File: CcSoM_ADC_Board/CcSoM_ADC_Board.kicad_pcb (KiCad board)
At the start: 4 copper layers, 160 x 100 mm, 159 parts, among them J1 SoM Connector, J12 USB_C_Receptacle_USB2.0_16P, J13 Conn_02x03_Odd_Even, J14 Conn_02x03_Odd_Even, J15 Conn_02x02_Counter_Clockwise, J16 Barrel_Jack, J18 USB_A, J19 USB_A, J3 Conn_02x8_Odd_Even, J4 Conn_Coaxial, J5 HR911130A1, J6 Conn_01x14, J7 Conn_01x08, J8 Conn_01x16_Socket, J9 Conn_01x08, SW3 SW_Push, U1 SN74LVC00APWE4, U10 USB3343, U11 RTL8211E-VB-CG, U12 LTC2242IUP-12-PBF, U14 SN74CB3T3306DCTR, U2 74AUP1G04, U3 93LC46B, U4 FT2232HL, U5 SN74CB3T3245PWR, U6 TPS73625DBV, U7 TPS3307-33DR, U8 TPS73633DBV, U9 TXS0202YZPR, X1 12MHz, Y1 25MHz

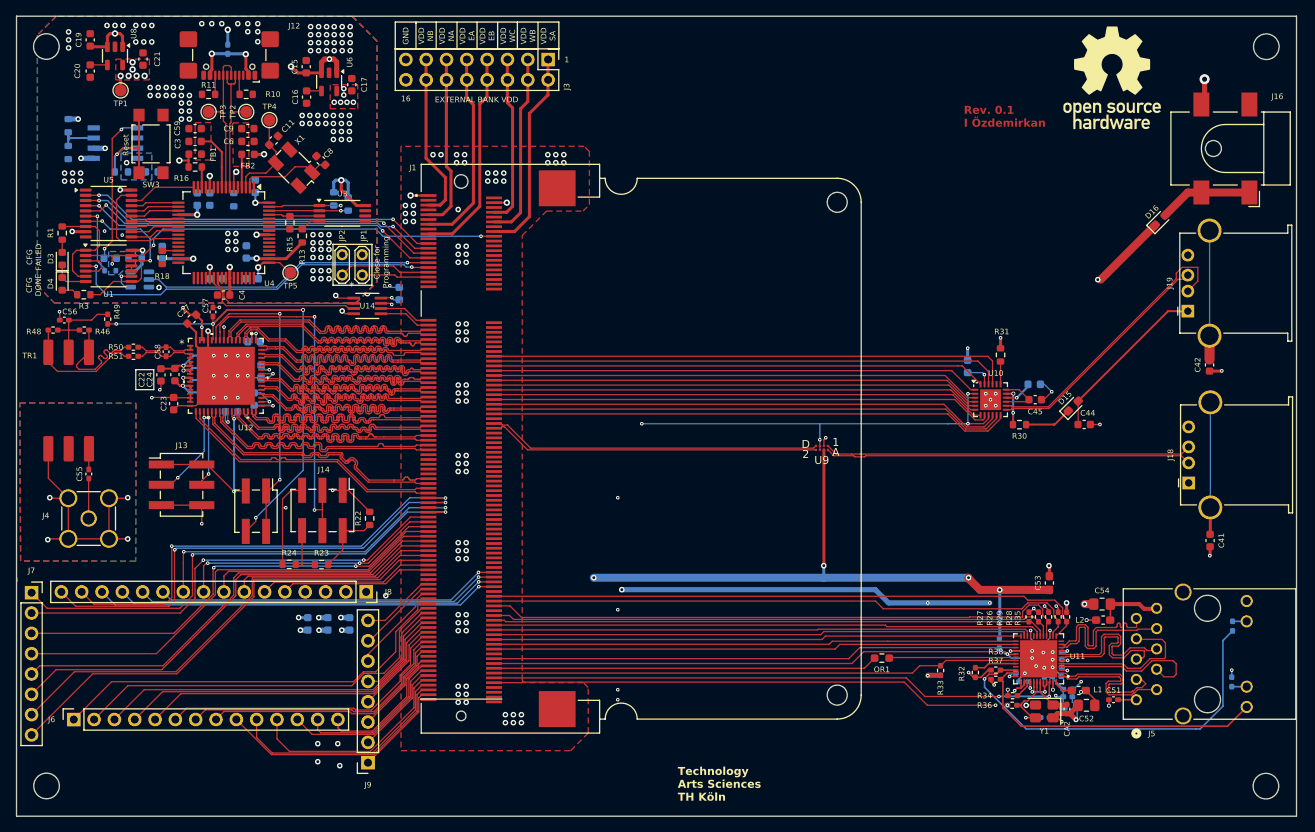
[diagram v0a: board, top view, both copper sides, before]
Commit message: changed schottky, began to add digikey part numbers
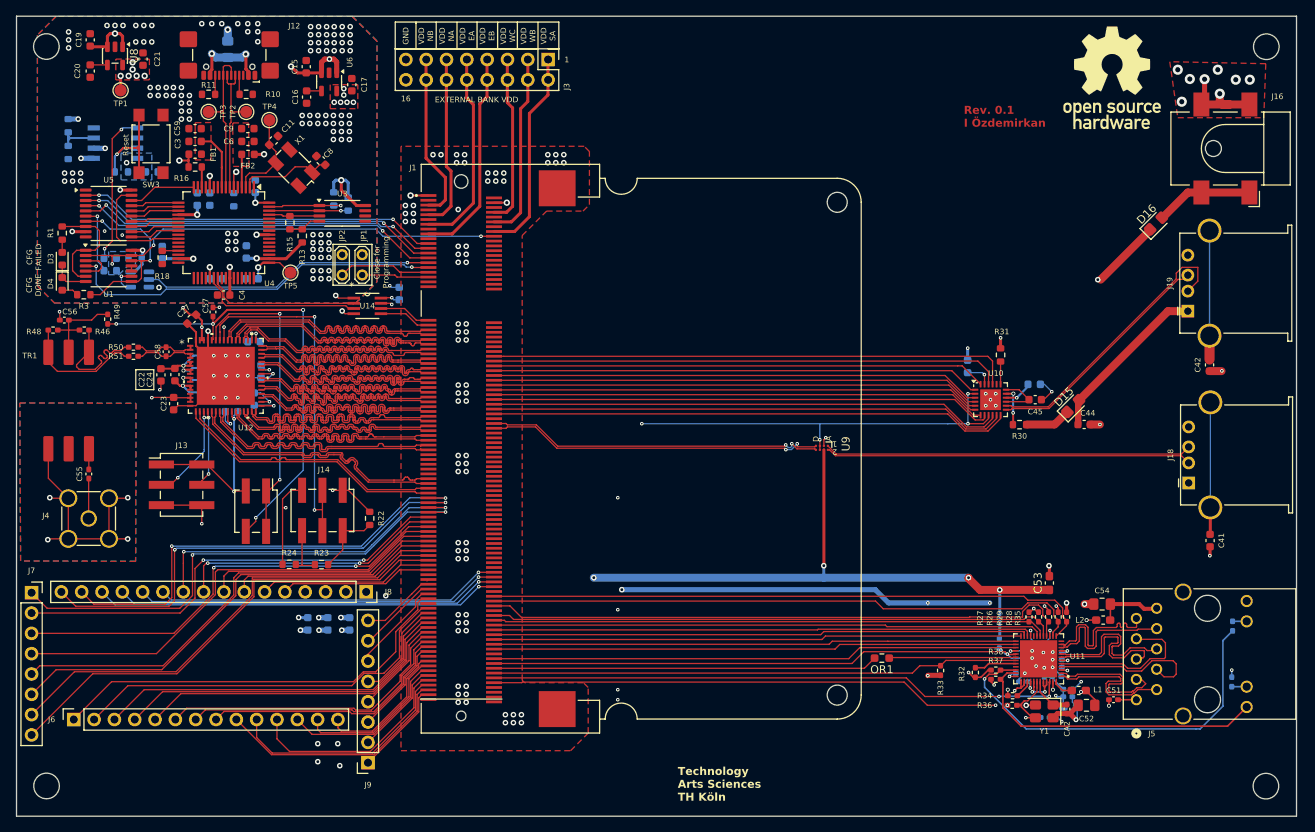
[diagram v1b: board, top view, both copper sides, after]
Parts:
- D1: footprint Diode_SMD:D_SOD-523 -> LED_SMD:LED_0603_1608Metric
- D15, D16: footprint Diode_SMD:D_0603_1608Metric_Pad1.05x0.95mm_HandSolder -> Diode_SMD:D_0805_2012Metric_Pad1.15x1.40mm_HandSolder
- D17: footprint Diode_SMD:D_0402_1005Metric_Pad0.77x0.64mm_HandSolder -> Diode_SMD:D_0805_2012Metric_Pad1.15x1.40mm_HandSolder
- moved D16 0.67 mm to (209.5, 76.5)
- turned R22 to -90 degrees
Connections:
- J16 pad 3: (no net) -> OGND
- J18 pad 2: /usb2/D_+ -> /usb2/D_-
- J18 pad 3: /usb2/D_- -> /usb2/D_+
- U9 pad A1: /usb2/D_- -> /usb2/D_+
- U9 pad A2: /usb2/D_+ -> /usb2/D_-
- U9 pad D1: USB2_- -> USB2_+
- U9 pad D2: USB2_+ -> USB2_-
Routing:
- net OGND: track 118.4 -> 128.0 mm, vias 260 -> 267
- net +5V: track 364.2 -> 362.9 mm
- net USB2_-: track 41.6 -> 42.3 mm, vias 0 -> 2
- net USB2_+: track 41.5 -> 42.2 mm, vias 0 -> 2
- net Net-(D16-A): track 12.1 -> 12.7 mm

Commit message: digikey no not complete
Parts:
- C44: value 3uF -> 3.3uF
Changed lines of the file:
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@@
 			)
 		)
-		(property "Datasheet" ""
+		(property "Datasheet" "~"
 			(at 0 0 180)
 			(layer "F.Fab")
@@
 			)
 		)
-		(property "Description" ""
+		(property "Description" "Resistor"
 			(at 0 0 180)
 			(layer "F.Fab")
@@
 			)
 		)
-		(property "Datasheet" ""
+		(property "Datasheet" "~"
 			(at 0 0 90)
 			(layer "F.Fab")
@@
 			)
 		)
-		(property "Description" ""
+		(property "Description" "Unpolarized capacitor, small symbol"
 			(at 0 0 90)
 			(layer "F.Fab")
@@
 			)
 		)
-		(property "Value" "3uF"
+		(property "Value" "3.3uF"
 			(at 0 1.43 0)
 			(layer "F.Fab")
@@
 		(tags "capacitor")
 		(property "Reference" "C43"
-			(at -0.232769 1.931116 90)
+			(at 0.017231 1.681116 90)
 			(layer "B.SilkS")
 			(effects
@@
 	)
 	(gr_text "Stackup: JLC041011-3313\n50Ohm Single-ended: 0.1427\n100Ohm differential:\n	width:0.1016 spacing:0.1524\n"
-		(at 133.2 121.45 0)
+		(at 133.2 119.25 0)
 		(layer "Cmts.User")
 		(effects

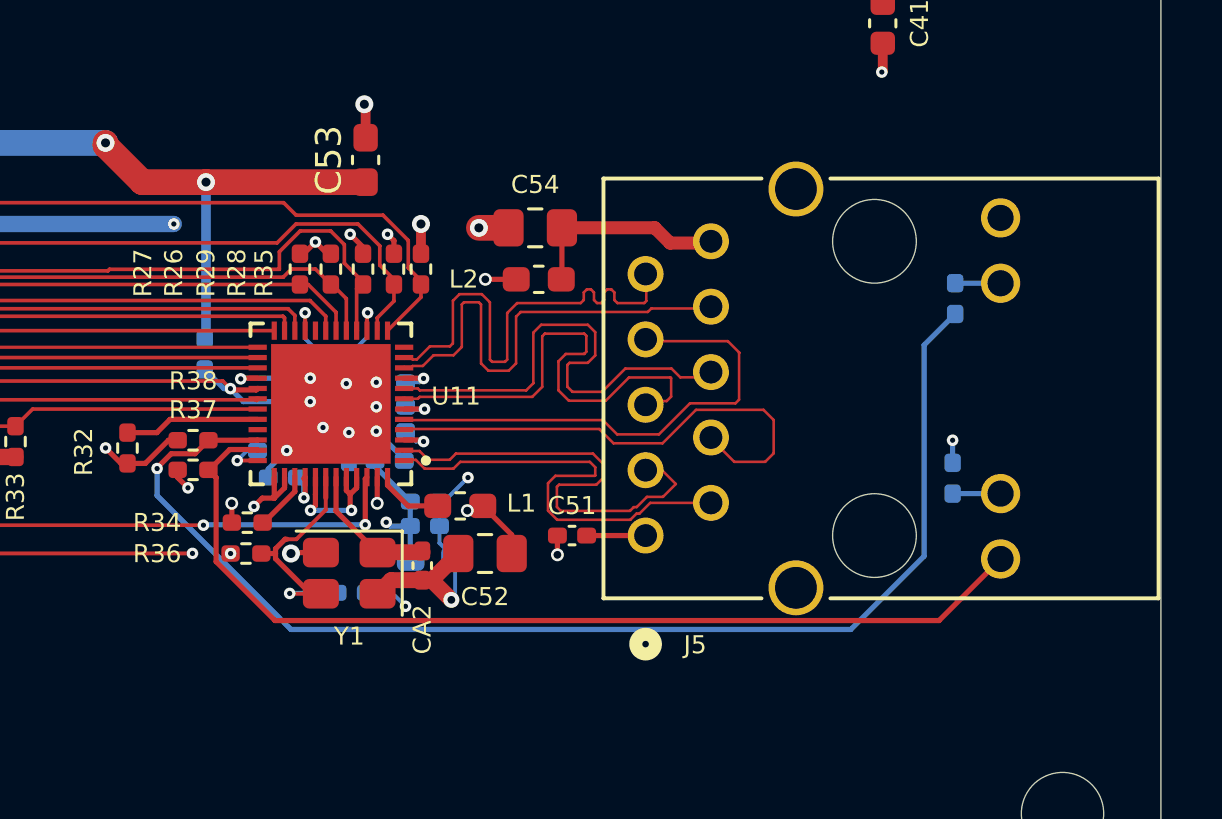
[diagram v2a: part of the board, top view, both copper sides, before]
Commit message: changed library path added symbols and footprints
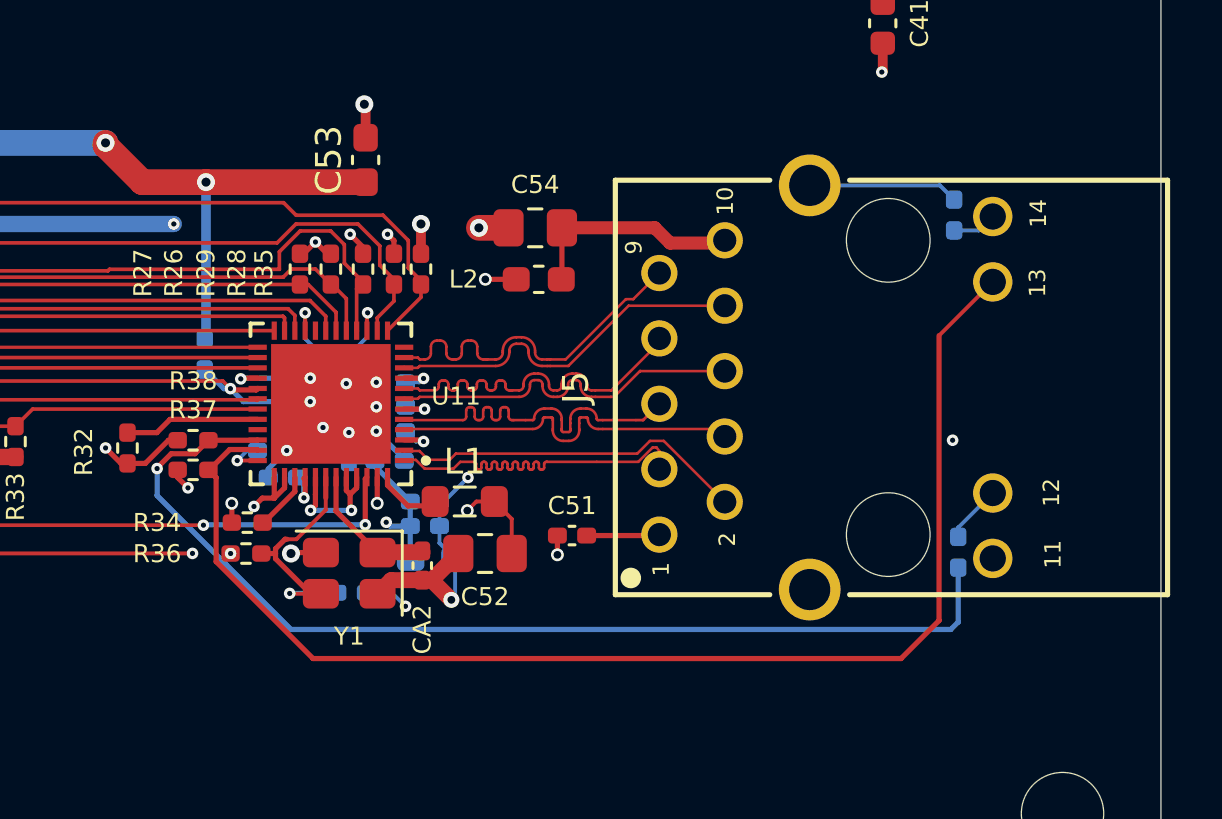
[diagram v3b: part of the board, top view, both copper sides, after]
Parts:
- removed R40: 510R R0402 5%, Resistor_SMD:R_0402_1005Metric_Pad0.72x0.64mm_HandSolder
- added R4: 510R R0402 5%, Resistor_SMD:R_0402_1005Metric_Pad0.72x0.64mm_HandSolder, B.Cu at (219.2, 136.7)
- J5: value HR911130A1 -> WE-RJ45_7498111124; footprint HR911130A1:HR911130A_HAN -> WE-RJ45_7498111124:7498111124
- L1: footprint Inductor_SMD:L_0603_1608Metric_Pad1.05x0.95mm_HandSolder -> Inductor_SMD:L_0805_2012Metric_Pad1.05x1.20mm_HandSolder
- moved J5 11.0 mm to (216.5, 130.2)
- moved R39 10.2 mm to (219.1, 123.6)
- moved L1 0.24 mm to (200.1, 134.7)
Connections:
- J5 pad 11: /gigabit_ethernet/LED1_AD1 -> +3V3
- J5 pad 12: /gigabit_ethernet/RGMII_GR- -> /gigabit_ethernet/RGMI_YE-
- J5 pad 13: /gigabit_ethernet/RGMI_YE- -> /gigabit_ethernet/LED1_AD1
- J5 pad 14: +3V3 -> /gigabit_ethernet/RGMII_GR-
- J5 pad 2: /gigabit_ethernet/MDI0_P -> /gigabit_ethernet/MDI0_N
- J5 pad 3: /gigabit_ethernet/MDI0_N -> /gigabit_ethernet/MDI0_P
- J5 pad 5: /gigabit_ethernet/MDI2_P -> /gigabit_ethernet/MDI1_N
- J5 pad 6: /gigabit_ethernet/MDI2_N -> /gigabit_ethernet/MDI2_P
- J5 pad 7: /gigabit_ethernet/MDI1_N -> /gigabit_ethernet/MDI2_N
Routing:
- net +3V3: track 469.0 -> 486.6 mm
- net /gigabit_ethernet/LED1_AD1: track 38.2 -> 50.1 mm
- net /gigabit_ethernet/LED0_AD0: track 48.5 -> 40.6 mm
- net /gigabit_ethernet/MDI1_N: track 19.5 -> 14.4 mm
- net /gigabit_ethernet/MDI1_P: track 19.5 -> 14.5 mm
- net OGND: track 128.0 -> 132.9 mm
- net /gigabit_ethernet/MDI2_N: track 19.1 -> 14.4 mm
- net /gigabit_ethernet/MDI2_P: track 19.1 -> 14.4 mm
- net /gigabit_ethernet/MDI3_N: track 18.5 -> 14.4 mm
- net /gigabit_ethernet/MDI3_P: track 18.5 -> 14.5 mm
- net /gigabit_ethernet/MDI0_N: track 18.2 -> 14.5 mm
- net /gigabit_ethernet/MDI0_P: track 17.9 -> 14.4 mm
- net VDD10_EPHY: track 30.6 -> 31.6 mm
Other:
- board text added: "U11"

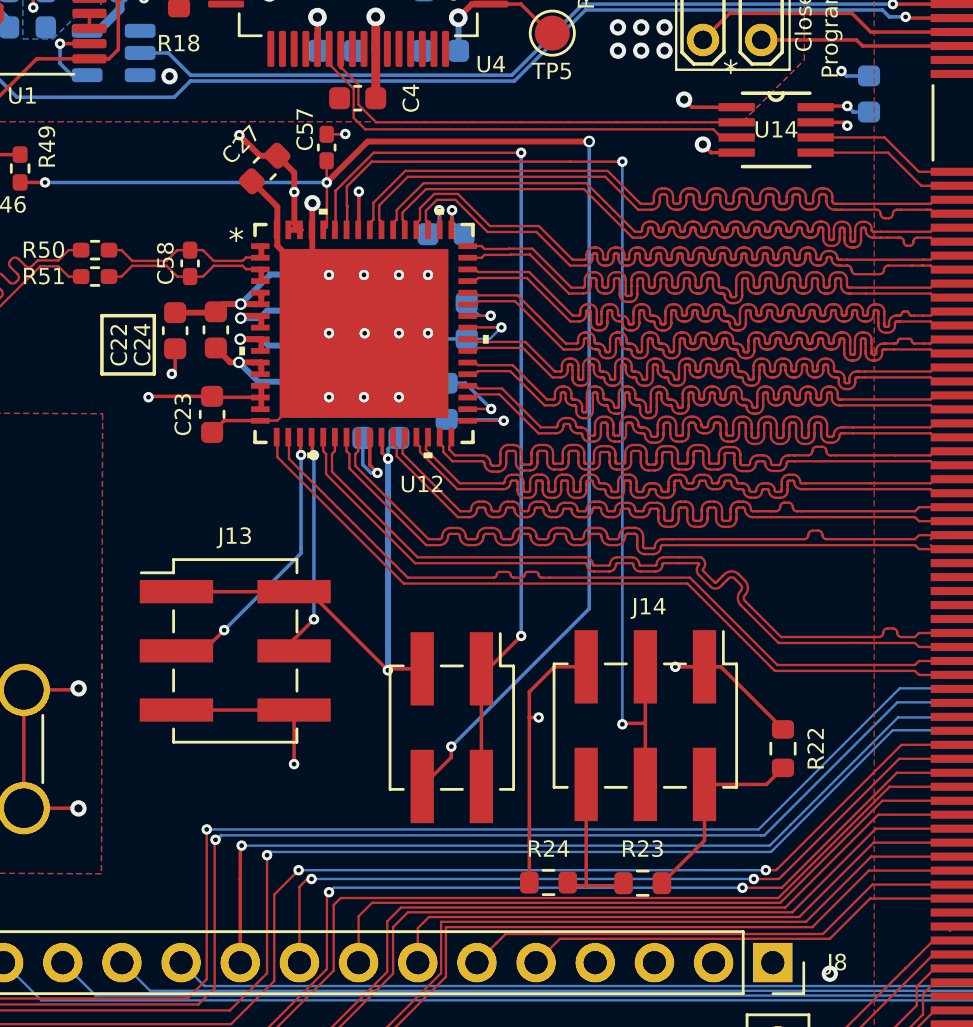
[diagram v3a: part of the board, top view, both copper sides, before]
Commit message: changed footprint of pinheader from smd to through hole
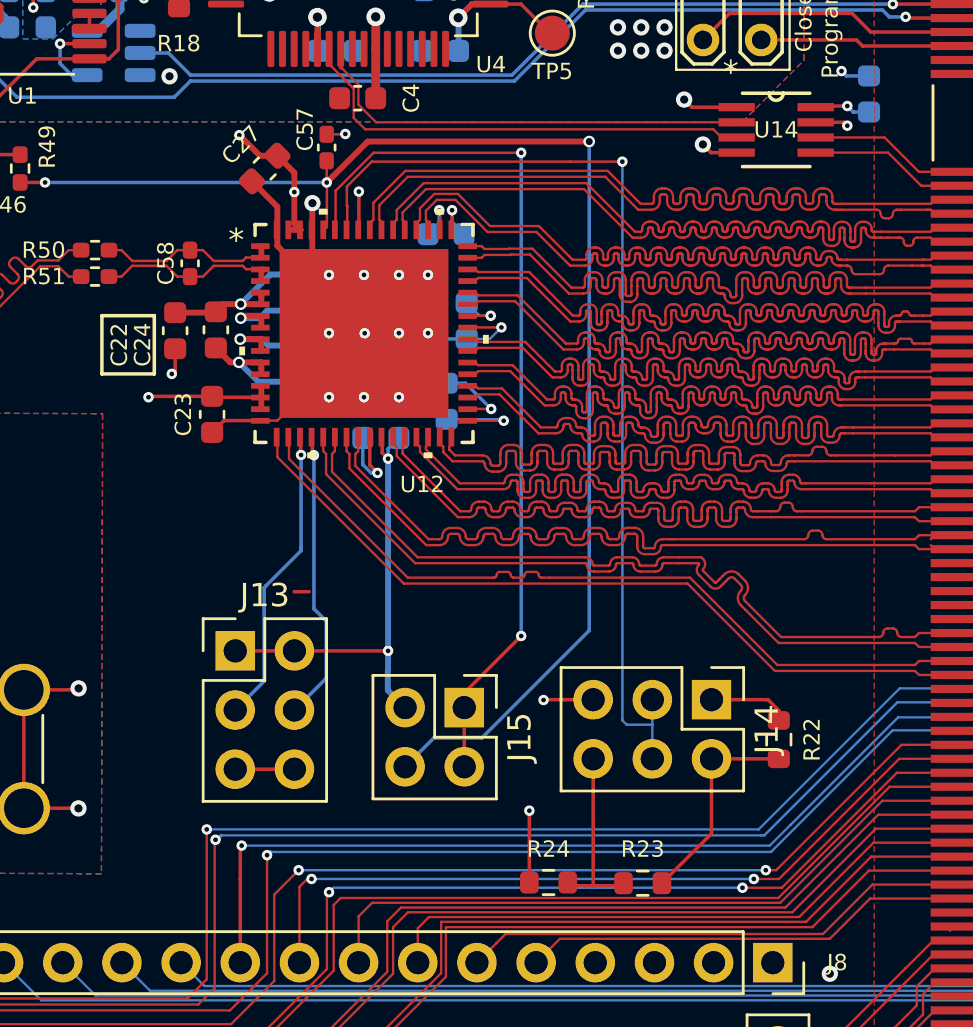
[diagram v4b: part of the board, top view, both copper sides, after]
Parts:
- J13, J14: footprint Connector_PinHeader_2.54mm:PinHeader_2x03_P2.54mm_Vertical_SMD -> Connector_PinHeader_2.54mm:PinHeader_2x03_P2.54mm_Vertical
- J15: footprint Connector_PinHeader_2.54mm:PinHeader_2x02_P2.54mm_Vertical_SMD -> Connector_PinHeader_2.54mm:PinHeader_2x02_P2.54mm_Vertical
- moved J14 3.05 mm to (108.2, 111.2)
- moved J15 1.01 mm to (97.6, 111.6)
- moved R22 0.43 mm to (111.1, 113.0)
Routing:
- net OGND: track 132.9 -> 121.7 mm
- net Net-(J13-Pin_4): track 9.58 -> 12.6 mm, vias 2 -> 1
- net Net-(J14-Pin_3): track 44.8 -> 42.0 mm, vias 2 -> 1
- net OVDD: track 538.9 -> 537.4 mm, vias 33 -> 32
- net Net-(J14-Pin_6): track 6.80 -> 7.89 mm
- net Net-(J14-Pin_2): track 8.66 -> 9.66 mm
- net Net-(J13-Pin_3): track 12.3 -> 13.0 mm, vias 2 -> 1
- net Net-(J15-Pin_1): track 38.4 -> 37.7 mm
- net V_CM: track 59.4 -> 59.6 mm, vias 4 -> 3
